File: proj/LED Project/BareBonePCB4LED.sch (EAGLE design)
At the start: 16 parts, among them J3 AVR_SPI_PROG_3X2NS, U1 R-78E5.0-1.0, Y1 16MHz

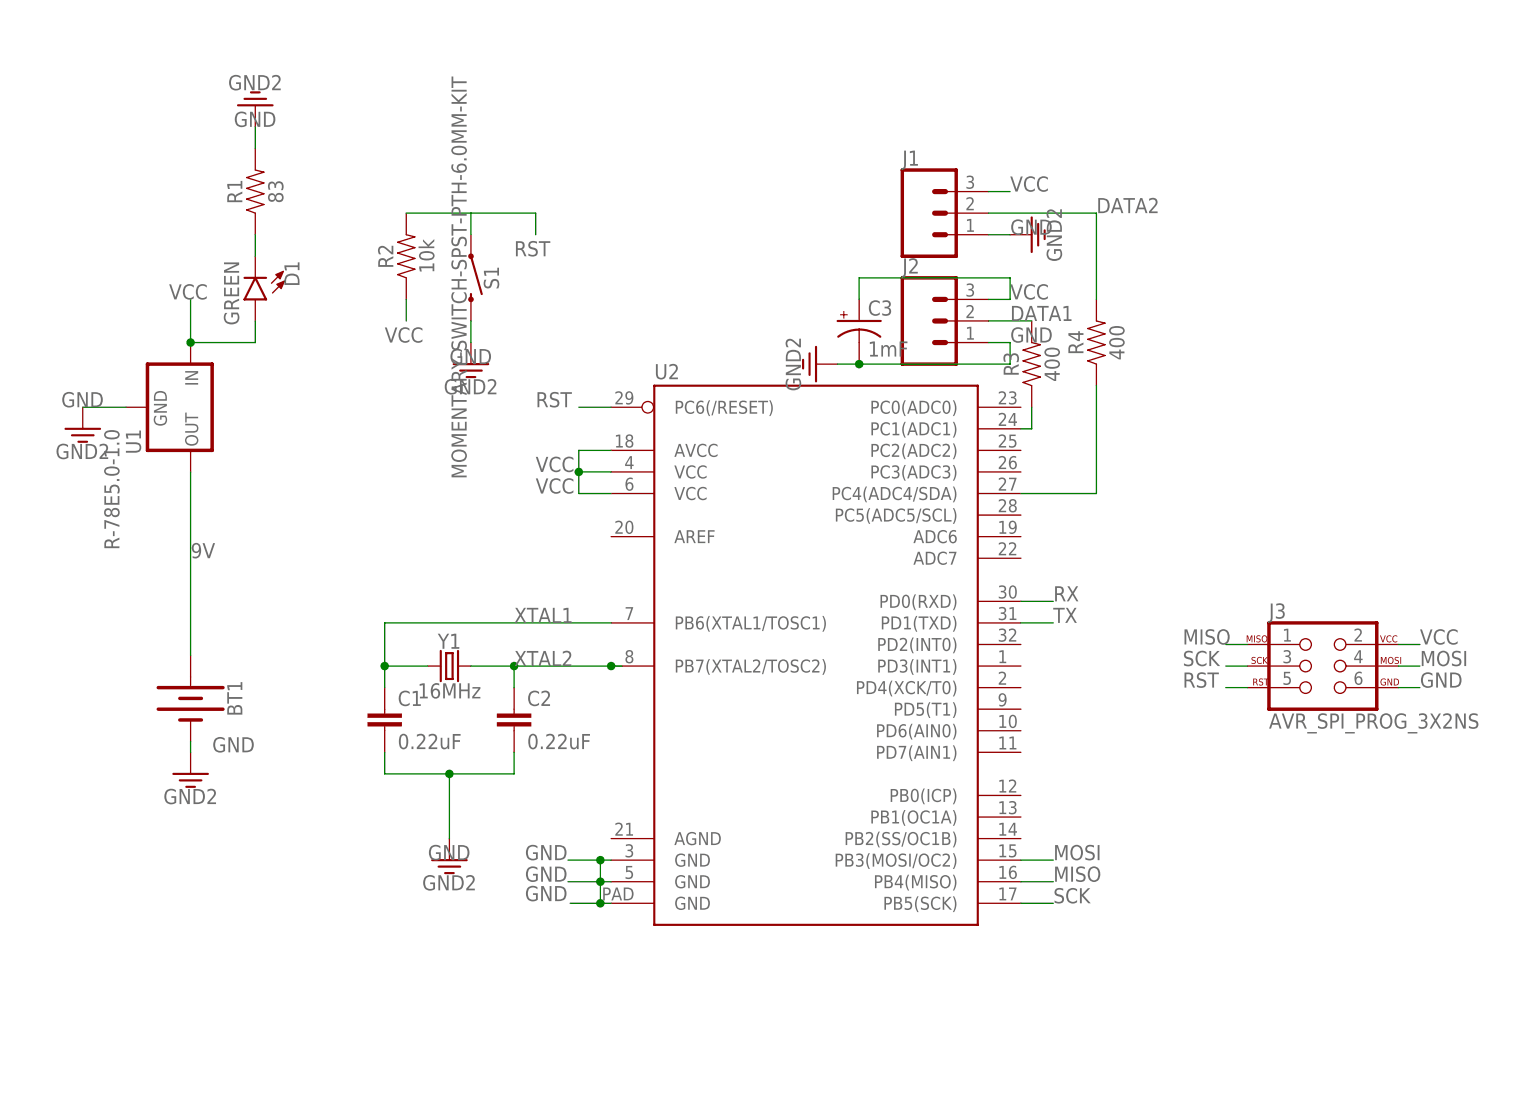
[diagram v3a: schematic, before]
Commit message: Cleaning LED Schematic + Board
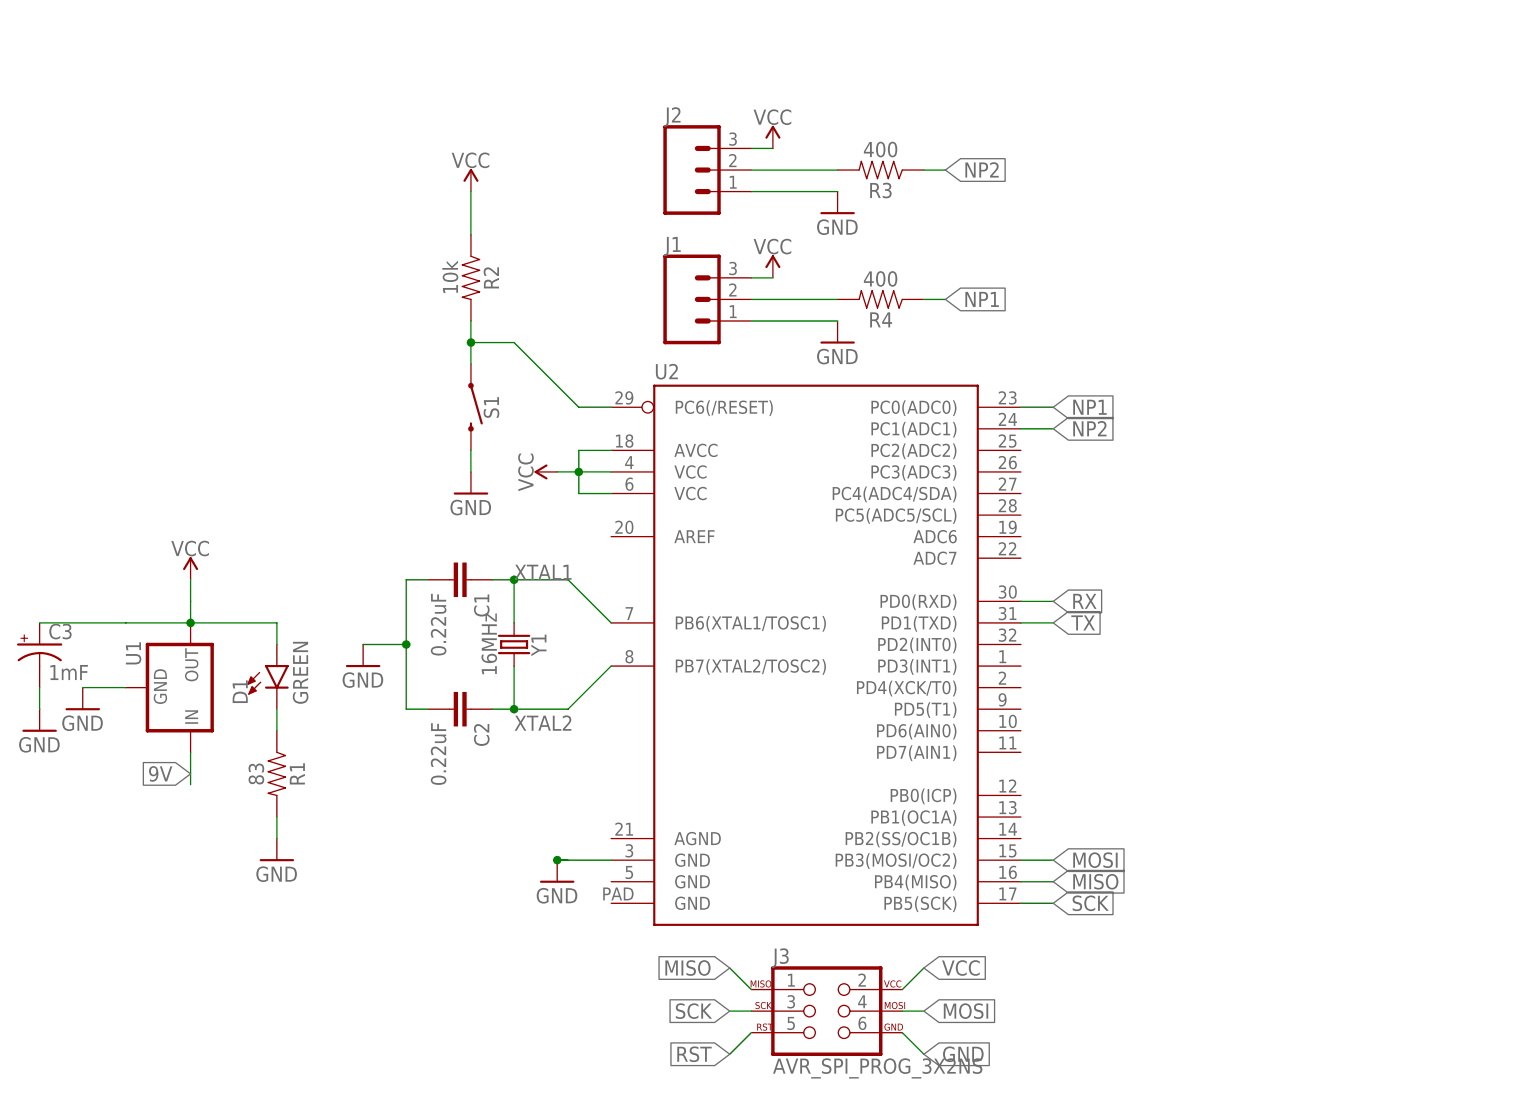
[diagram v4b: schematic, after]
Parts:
- removed BT1: (no value), SparkFun-Batteries:BATTERY-9V
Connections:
- net N$7 renamed NP2
- removed net DATA: R4.1, U2.PC4(ADC4/SDA)
- new net NP1: R4.1, U2.PC0(ADC0)
- net 9V: now also U1.IN; no longer BT1.+, U1.OUT
- net DATA1: now also J1.2, R4.2; no longer J2.2, R3.2
- net DATA2: now also J2.2, R3.2; no longer J1.2, R4.2
- net GND: no longer BT1.-, U2.GND@5, U2.GND@PAD
- net VCC: now also U1.OUT; no longer U1.IN
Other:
- moved on the sheet: C1, C2, C3, D1, J1, J2, J3, R1, R2, R3, R4, S1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
